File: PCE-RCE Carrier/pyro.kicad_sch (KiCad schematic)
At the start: 17 parts, among them J5 TBL002A-350-08GY-2GY, Q1 2SD2537, Q2 2SD2537, Q3 2SD2537, Q4 2SD2537

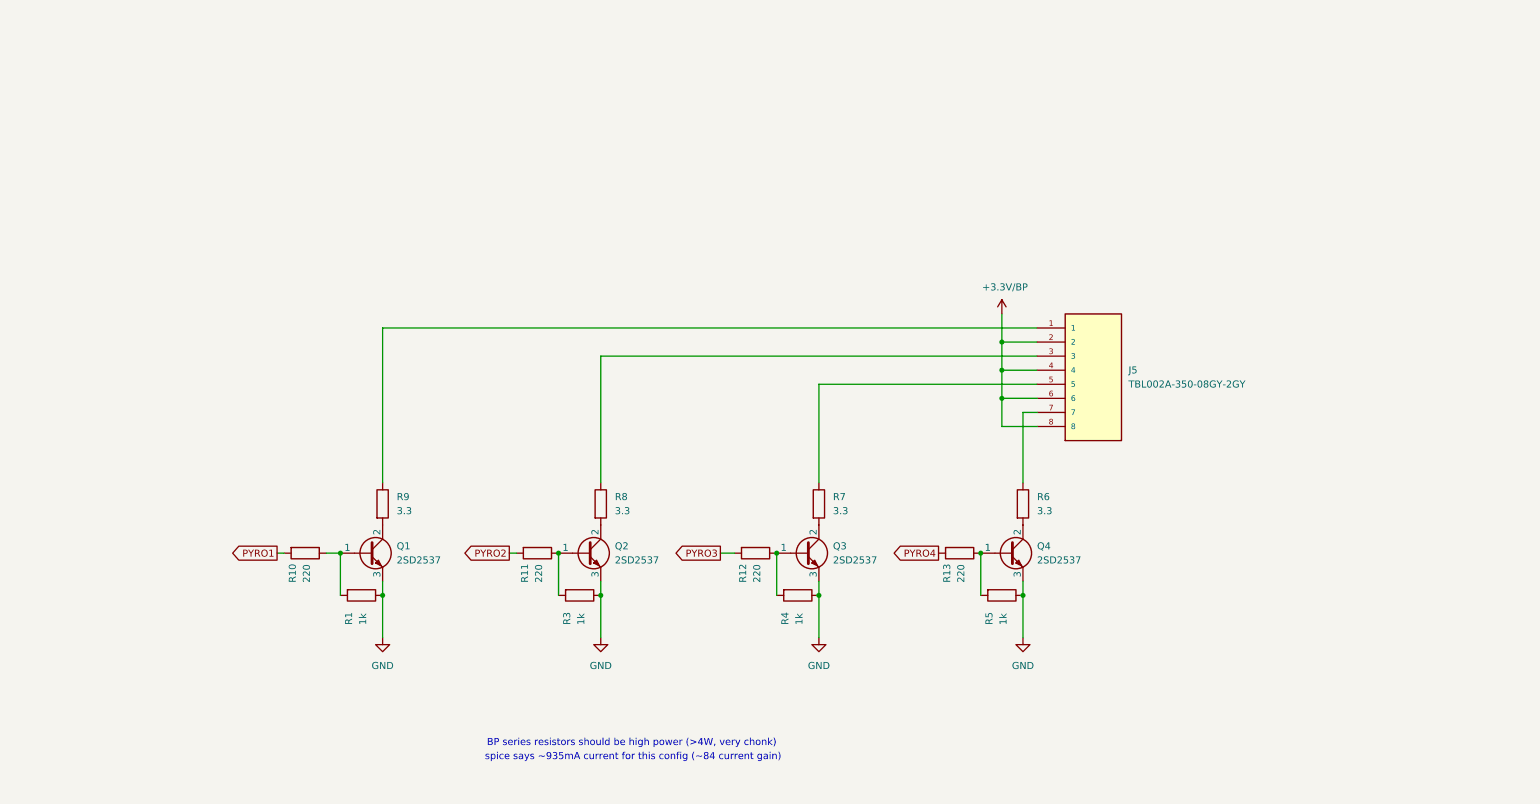
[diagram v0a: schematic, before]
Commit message: restructured airdahl for carrier boards, switched 20 pin debug jtag for 10 pin for use with adafruit usb stlink, schematic formatting
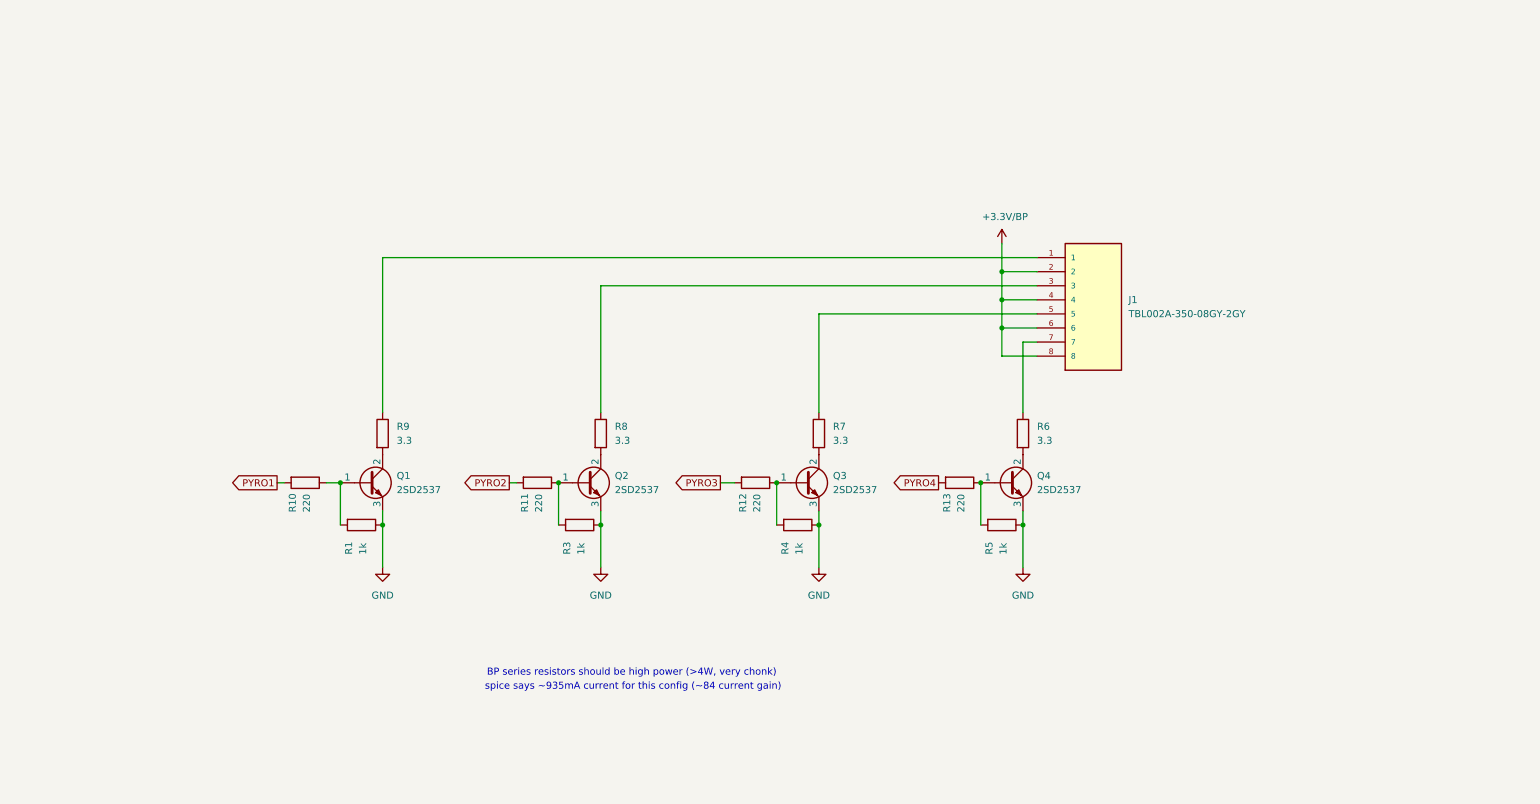
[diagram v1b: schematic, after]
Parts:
- removed J5: TBL002A-350-08GY-2GY, TBL002A-350-08GY-2GY:CUI_TBL002A-350-08GY-2GY, symbol TBL002A-350-08GY-2GY:TBL002A-350-08GY-2GY
- added J1: TBL002A-350-08GY-2GY, TBL002A-350-08GY-2GY:CUI_TBL002A-350-08GY-2GY, symbol TBL002A-350-08GY-2GY:TBL002A-350-08GY-2GY
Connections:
- net +3.3V/BP: now also J1.2, J1.4, J1.6, J1.8
- net at R6.1: now also J1.7
- net at R8.1: now also J1.3
- net at R7.1: now also J1.5
- net at R9.1: now also J1.1
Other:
- company: (none) -> Washington University in St. Louis
- title: (none) -> RCE Pyro Charges

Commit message: H-Bridge wiring + motor ports, cleaned up carrier schematics, added MISO source terminating resistors on carriers
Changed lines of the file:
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@@
 		)
 	)
-	(global_label "PYRO2"
-		(shape output)
+	(hierarchical_label "PYRO2"
+		(shape input)
 		(at 104.14 102.87 180)
-		(fields_autoplaced yes)
 		(effects
 			(font
@@
 			(justify right)
 		)
-		(property "Intersheetrefs" "${INTERSHEET_REFS}"
-			(at 94.9862 102.87 0)
-			(hide yes)
-			(show_name no)
-			(do_not_autoplace no)
-			(effects
-				(font
-					(size 1.27 1.27)
-				)
-				(justify right)
-			)
-		)
 	)
-	(global_label "PYRO4"
-		(shape output)
-		(at 181.61 102.87 180)
-		(fields_autoplaced yes)
+	(hierarchical_label "PYRO1"
+		(shape input)
+		(at 62.23 102.87 180)
 		(effects
 			(font
@@
 			(justify right)
 		)
-		(property "Intersheetrefs" "${INTERSHEET_REFS}"
-			(at 172.4562 102.87 0)
-			(hide yes)
-			(show_name no)
-			(do_not_autoplace no)
-			(effects
-				(font
-					(size 1.27 1.27)
-				)
-				(justify right)
-			)
-		)
 	)
-	(global_label "PYRO1"
-		(shape output)
-		(at 62.23 102.87 180)
-		(fields_autoplaced yes)
+	(hierarchical_label "PYRO4"
+		(shape input)
+		(at 181.61 102.87 180)
 		(effects
 			(font
@@
 			(justify right)
 		)
-		(property "Intersheetrefs" "${INTERSHEET_REFS}"
-			(at 53.0762 102.87 0)
-			(hide yes)
-			(show_name no)
-			(do_not_autoplace no)
-			(effects
-				(font
-					(size 1.27 1.27)
-				)
-				(justify right)
-			)
-		)
 	)
-	(global_label "PYRO3"
-		(shape output)
+	(hierarchical_label "PYRO3"
+		(shape input)
 		(at 142.24 102.87 180)
-		(fields_autoplaced yes)
 		(effects
 			(font
@@
 			(justify right)
 		)
-		(property "Intersheetrefs" "${INTERSHEET_REFS}"
-			(at 133.0862 102.87 0)
-			(hide yes)
-			(show_name no)
-			(do_not_autoplace no)
-			(effects
-				(font
-					(size 1.27 1.27)
-				)
-				(justify right)
-			)
-		)
 	)

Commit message: carrier board comments
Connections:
- net PYRO1 renamed PYRO_1
- net PYRO2 renamed PYRO_2
- net PYRO3 renamed PYRO_3
- net PYRO4 renamed PYRO_4
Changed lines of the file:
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@@
 		)
 	)
-	(hierarchical_label "PYRO2"
+	(hierarchical_label "PYRO_2"
 		(shape input)
 		(at 104.14 102.87 180)
@@
 		)
 	)
-	(hierarchical_label "PYRO1"
+	(hierarchical_label "PYRO_1"
 		(shape input)
 		(at 62.23 102.87 180)
@@
 		)
 	)
-	(hierarchical_label "PYRO4"
+	(hierarchical_label "PYRO_4"
 		(shape input)
 		(at 181.61 102.87 180)
@@
 		)
 	)
-	(hierarchical_label "PYRO3"
+	(hierarchical_label "PYRO_3"
 		(shape input)
 		(at 142.24 102.87 180)

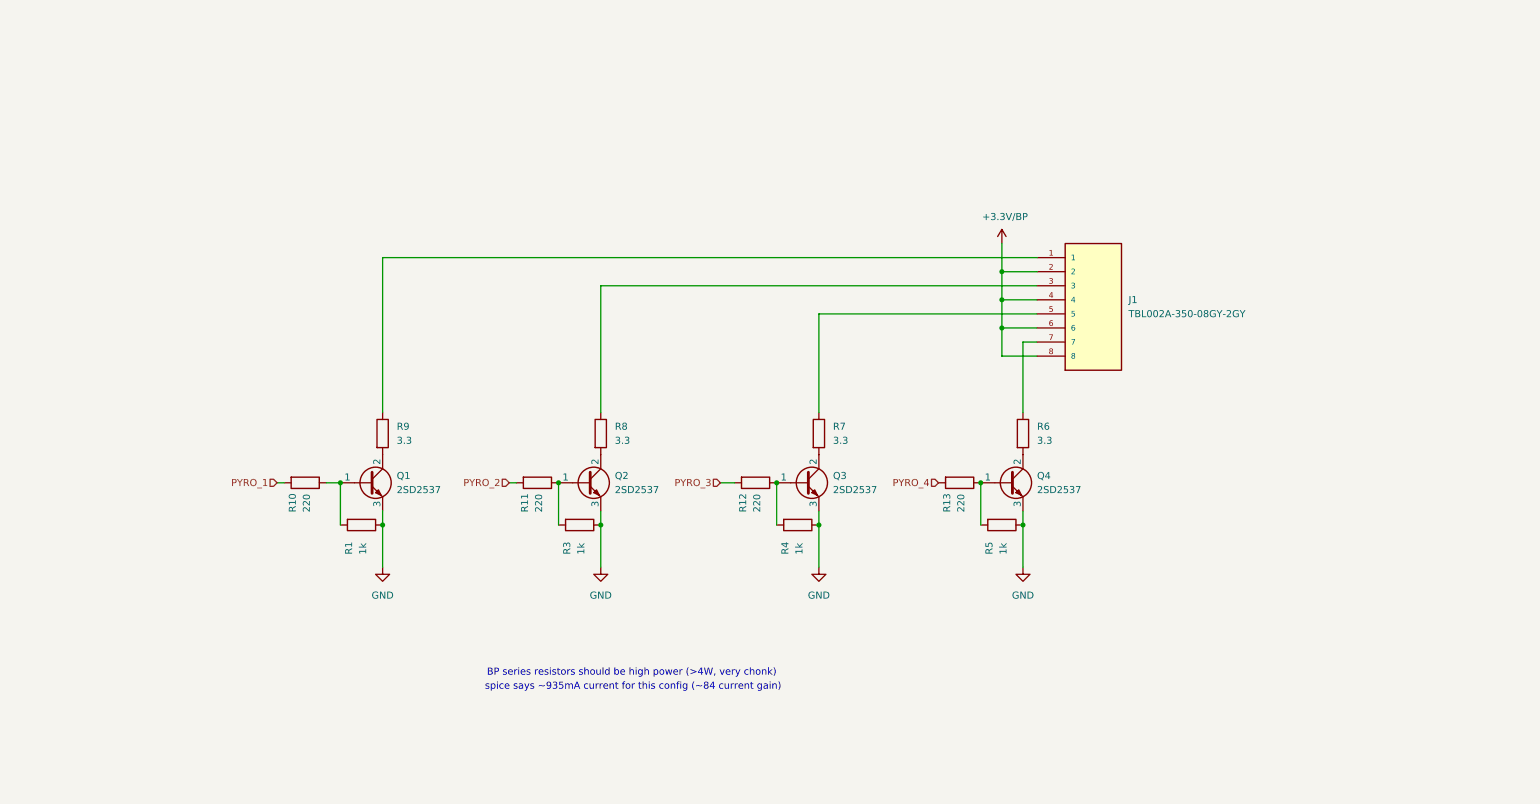
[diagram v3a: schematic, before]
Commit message: updated pyro circuit to be like easymini, lowk will prob make it a separate carrier
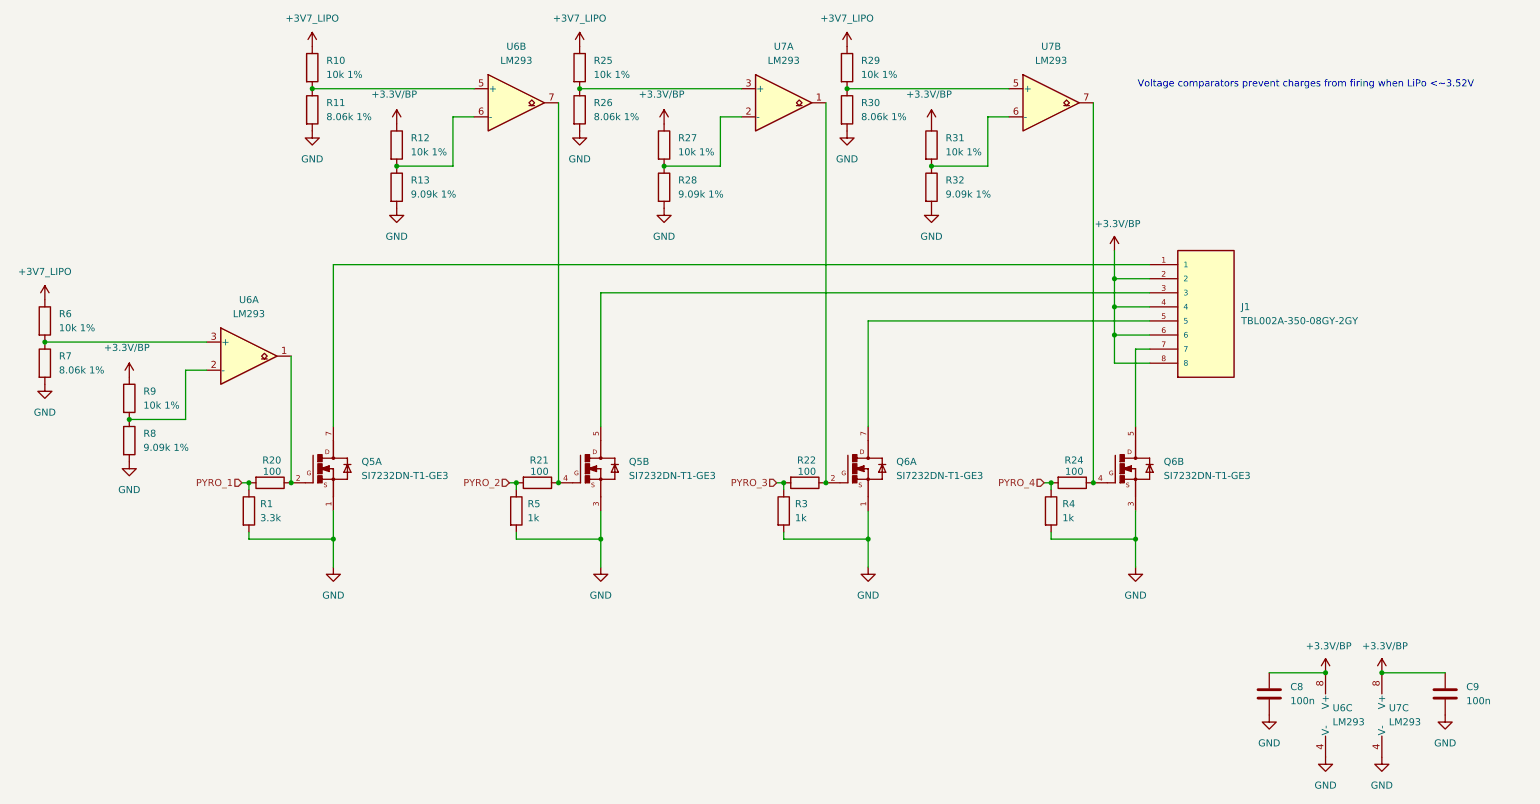
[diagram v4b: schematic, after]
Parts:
- removed Q1, Q2, Q3, Q4: 2SD2537, Package_TO_SOT_SMD:SOT-89-3, symbol Simulation_SPICE:NPN
- added C8, C9: 100n, Capacitor_SMD:C_0402_1005Metric, symbol Device:C
- added Q5, Q6: SI7232DN-T1-GE3, Si7232DN:TRANS_SI7232DN-T1-GE3, symbol SI7232DN-T1-GE3:SI7232DN-T1-GE3
- added R20, R21, R22, R24: 100, Resistor_SMD:R_0603_1608Metric, symbol Device:R
- added R25, R27, R29, R31: 10k 1%, Resistor_SMD:R_0402_1005Metric, symbol Device:R
- added R26, R30: 8.06k 1%, Resistor_SMD:R_0402_1005Metric, symbol Device:R
- added R28, R32: 9.09k 1%, Resistor_SMD:R_0402_1005Metric, symbol Device:R
- added U6, U7: LM293, Package_SO:VSSOP-8_3x3mm_P0.65mm, symbol Comparator:LM393
- R1: value 1k -> 3.3k
- R10, R12: value 220 -> 10k 1%; footprint Resistor_SMD:R_0603_1608Metric -> Resistor_SMD:R_0402_1005Metric
- R11: value 220 -> 8.06k 1%; footprint Resistor_SMD:R_0603_1608Metric -> Resistor_SMD:R_0402_1005Metric
- R13: value 220 -> 9.09k 1%; footprint Resistor_SMD:R_0603_1608Metric -> Resistor_SMD:R_0402_1005Metric
- R6, R9: value 3.3 -> 10k 1%; footprint Resistor_SMD:R_2512_6332Metric -> Resistor_SMD:R_0402_1005Metric
- R7: value 3.3 -> 8.06k 1%; footprint Resistor_SMD:R_2512_6332Metric -> Resistor_SMD:R_0402_1005Metric
- R8: value 3.3 -> 9.09k 1%; footprint Resistor_SMD:R_2512_6332Metric -> Resistor_SMD:R_0402_1005Metric
- renumbered R4 to R3, R5 to R4, R3 to R5
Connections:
- net +3.3V/BP: now also R12.1, R9.1, C8.1, C9.1, R27.1, R31.1, U6.8 (V+), U7.8 (V+)
- net GND: now also R1.2, R11.2, R13.2, R3.2, R4.2, R5.2, R7.2, R8.2, C8.2, C9.2, Q5.1, Q5.3, Q6.1, Q6.3, R26.2, R28.2, R30.2, R32.2, U6.4 (V-), U7.4 (V-); no longer R1.1, R3.1, R4.1, R5.1
- net PYRO_1: now also R1.1, R20.2; no longer R10.2
- net PYRO_2: now also R5.1, R21.2; no longer R11.2
- net PYRO_3: now also R3.1, R22.2; no longer R12.2
- net PYRO_4: now also R4.1, R24.2; no longer R13.2
- net at J1.3: now also Q5.5, Q5.6; no longer R8.1
- net at R13.1: now also R12.2, U6.6 (-); no longer R4.2
- net at R6.2: now also R7.1, U6.3 (+)
- net at J1.7: now also Q6.5, Q6.6; no longer R6.1
- net at R11.1: now also R10.2, U6.5 (+); no longer R5.2
- net +3V7_LIPO: now reaches R10.1
- net +3V7_LIPO: now also R6.1, R25.1, R29.1; no longer R1.2
- net at J1.5: now also Q6.7, Q6.8; no longer R7.1
- net at J1.1: now also Q5.7, Q5.8; no longer R9.1
- net at R9.2: now also R8.1, U6.2 (-)
- new net: Q6.4, R24.1, U7.7
- new net: R25.2, R26.1, U7.3 (+)
- new net: R29.2, R30.1, U7.5 (+)
- new net: Q6.2, R22.1, U7.1
- new net: Q5.4, R21.1, U6.7
- new net: Q5.2, R20.1, U6.1
- new net: R27.2, R28.1, U7.2 (-)
- new net: R31.2, R32.1, U7.6 (-)
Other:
- note added: "Voltage comparators prevent charges from firing when LiPo <~3.52V"
- note removed: "BP series resistors should be high power (>4W, very chonk)"
- note removed: "spice says ~935mA current for this config (~84 current gain)"
- moved on the sheet: J1, R1, R3, R4, R5
